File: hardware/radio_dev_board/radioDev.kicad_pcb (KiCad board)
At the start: 4 copper layers, 100 x 75 mm, 98 parts, among them J1 Conn_02x03_Odd_Even, J2 Conn_01x05, J3 Conn_01x05, J4 USB_C_Receptacle_USB2.0V1, J5 Barrel_Jack_MountingPin, J6 USB_C_Receptacle_USB2.0V1, Q1 Q_NPN_CBE, SW1 Reset, U1 SP3485CN, U10 LM1117-3.3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

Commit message: added program and misc buttons. Finish layout
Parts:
- added C32: 0.1, Capacitor_SMD:C_0603_1608Metric_Pad1.05x0.95mm_HandSolder, F.Cu at (159.1, 99.8)
- added G***: LOGO, libraries:4i_small_inv, F.Cu at (214.2, 118.0)
- added R27: 100K, Resistor_SMD:R_0603_1608Metric_Pad1.05x0.95mm_HandSolder, F.Cu at (204.8, 125.9)
- added R28: 100K, Resistor_SMD:R_0603_1608Metric_Pad1.05x0.95mm_HandSolder, F.Cu at (179.6, 125.9)
- added SW2: SW_Push, Button_Switch_SMD:SW_SPST_PTS645, F.Cu at (172.6, 129.1)
- added SW3: PGM, Button_Switch_SMD:SW_SPST_PTS645, F.Cu at (197.6, 129.1)
- added SW4: Misc, Button_Switch_SMD:SW_SPST_PTS645, F.Cu at (186.4, 129.1)
- D3: value OP1 -> 13
- D4: value OP2 -> A3
- D5: value OP3 -> A2
- D6: value OP4 -> A1
- D7: value OP5 -> A0
- moved R24 19.9 mm to (160.3, 127.0)
- moved D13 16.9 mm to (162.7, 131.2), turned to 270 degrees
- moved R23 16.7 mm to (162.7, 127.0)
- moved D14 16.7 mm to (160.3, 131.2), turned to 270 degrees
- moved R20 8.53 mm to (216.8, 83.3), turned to 180 degrees
- moved C2 7.19 mm to (152.4, 108.0), turned to 180 degrees
- moved R2 1.33 mm to (206.8, 86.5)
- moved C30 1.20 mm to (152.7, 121.7)
- moved R3 1.20 mm to (193.4, 85.0)
- moved C28 1.20 mm to (152.7, 125.1)
- moved C29 1.20 mm to (152.7, 123.4)
- moved C6 1.10 mm to (171.9, 103.6)
- moved C4 0.90 mm to (157.5, 104.2)
- moved U5 0.45 mm to (186.0, 101.5)
- moved C9 0.35 mm to (183.3, 106.0)
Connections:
- C5 pad 1: /~Reset -> /Arduino Controller/~Reset
- R8 pad 2: /~Reset -> /Arduino Controller/~Reset
- SW1 pad 1: /~Reset -> /Arduino Controller/~Reset
- U2 pad B14: (no net) -> /A4
- U4 pad 11: (no net) -> /A4
- U4 pad 12: (no net) -> Net-(R28-Pad2)
- U4 pad 13: (no net) -> Net-(R27-Pad2)
- U4 pad 29: /~Reset -> /Arduino Controller/~Reset
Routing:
- net /TXD: track 0.00 -> 71.6 mm, vias 0 -> 2
- net /RXD: track 0.00 -> 71.6 mm, vias 0 -> 2
- net /A4: track 0.00 -> 60.4 mm, vias 0 -> 2
- net Net-(R27-Pad2): track 0.00 -> 55.8 mm, vias 0 -> 2
- net /Arduino Controller/~Reset: track 0.00 -> 49.7 mm, vias 0 -> 2
- net /MOSI: track 12.1 -> 61.3 mm, vias 0 -> 1
- net /MISO: track 18.0 -> 64.0 mm, vias 0 -> 1
- net Net-(R28-Pad2): track 0.00 -> 45.6 mm, vias 0 -> 2
- net /SCK: track 30.8 -> 74.2 mm, vias 0 -> 1
- net GND: track 90.6 -> 120.8 mm, vias 55 -> 62
- net Net-(R23-Pad1): track 0.00 -> 20.4 mm
- net Net-(R24-Pad1): track 0.00 -> 18.6 mm
- net Net-(C27-Pad1): track 0.00 -> 12.2 mm
- net +5V: track 114.2 -> 121.8 mm, vias 16 -> 27
- net +3V3: track 66.2 -> 73.2 mm, vias 14 -> 15
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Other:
- board text added: "+5V"
- board text added: "13"
- board text added: "4i Systems"
- board text added: "A0"
- board text added: "A1"
- board text added: "A2"
- board text added: "A3"
- board text added: "DC 8-28V"
- board text added: "GND"
- board text added: "Local"
- board text added: "MISO"
- board text added: "MOSI"
- board text added: "Misc"
- board text added: "PGM"
- board text added: "RX"
- board text added: "Radio"
- board text added: "SCK"
- board text added: "TART 3 Development Board (c) Phill Brown 2019"
- board text added: "TX"
- board text added: "~Reset"
- board text added: "~Reset~-Local"
- board text added: "~Reset~-Radio"

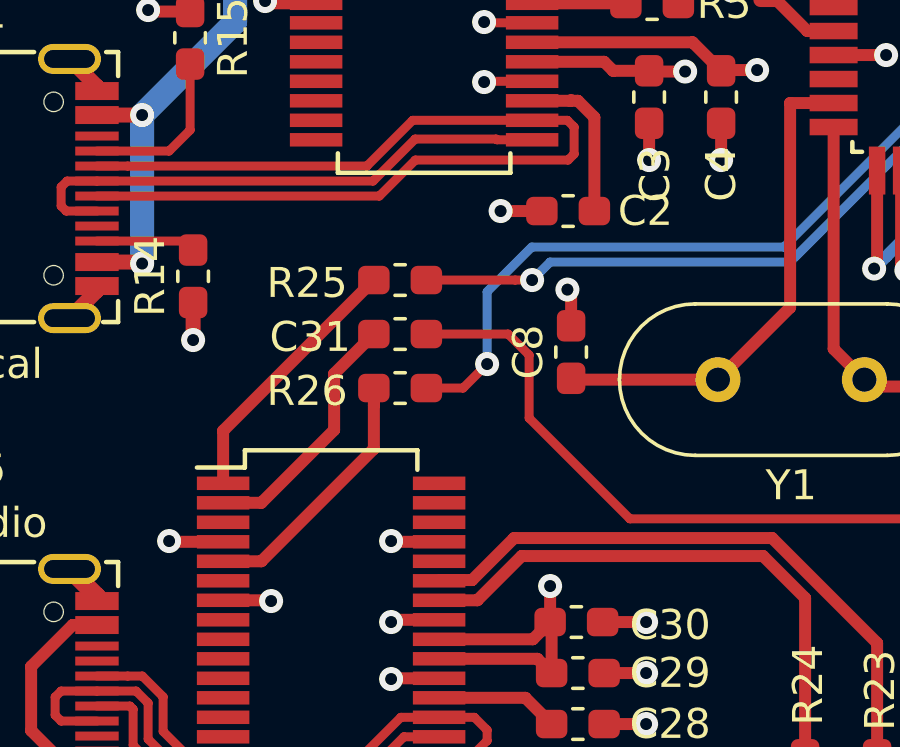
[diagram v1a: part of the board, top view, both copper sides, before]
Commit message: radio hub board started
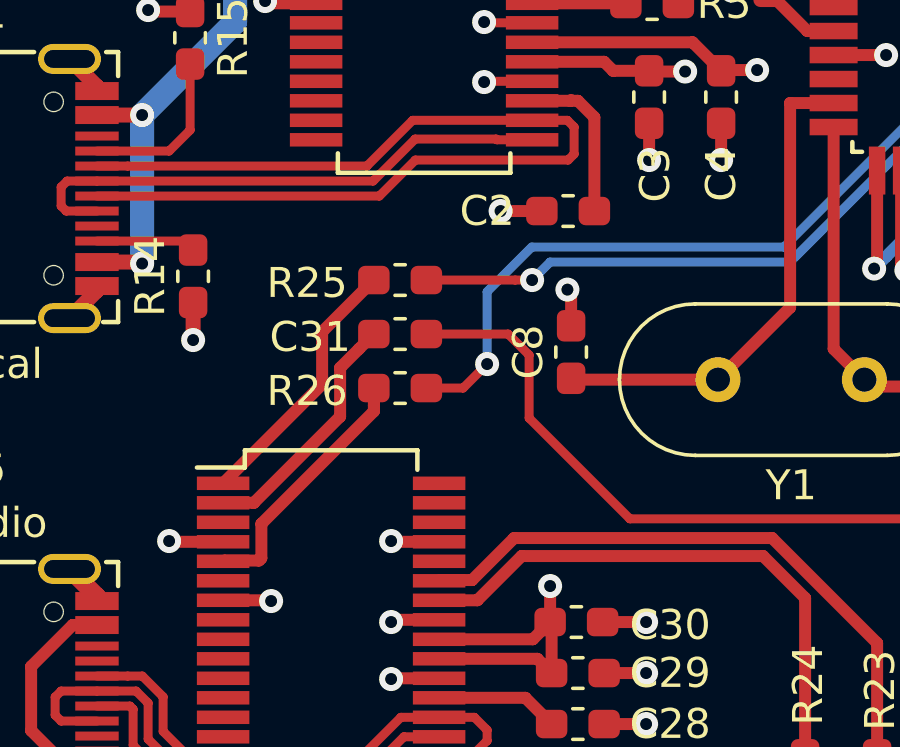
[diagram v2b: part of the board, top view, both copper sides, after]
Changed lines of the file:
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@@
-(kicad_pcb (version 20171130) (host pcbnew 5.1.4+dfsg1-2)
+(kicad_pcb (version 20171130) (host pcbnew 5.1.5+dfsg1-2)
   (general
     (thickness 1)
     (drawings 26)
-    (tracks 1005)
+    (tracks 1011)
     (zones 0)
     (modules 105)
@@
   )
   (setup
-    (last_trace_width 0.4)
+    (last_trace_width 0.25)
     (user_trace_width 0.2)
     (user_trace_width 0.3)
@@
       (outputformat 1)
       (mirror false)
-      (drillshape 1)
+      (drillshape 0)
       (scaleselection 1)
-      (outputdirectory ""))
+      (outputdirectory "eng/"))
   )
   (net 0 "")
@@
     (tags "capacitor handsolder")
     (attr smd)
-    (fp_text reference C2 (at -2.575 0) (layer F.SilkS)
+    (fp_text reference C2 (at 2.7 0) (layer F.SilkS)
       (effects (font (size 1 1) (thickness 0.15)))
     )
@@
   (segment (start 150.975 124.225) (end 151.85 125.1) (width 0.4) (layer F.Cu) (net 72))
   (segment (start 148.1 124.225) (end 150.975 124.225) (width 0.4) (layer F.Cu) (net 72))
-  (segment (start 142.175 117.725) (end 144.6 115.3) (width 0.4) (layer F.Cu) (net 73))
-  (segment (start 140.9 117.725) (end 142.175 117.725) (width 0.4) (layer F.Cu) (net 73))
-  (segment (start 144.6 113.425) (end 145.925 112.1) (width 0.4) (layer F.Cu) (net 73))
-  (segment (start 144.6 115.3) (end 144.6 113.425) (width 0.4) (layer F.Cu) (net 73))
+  (segment (start 141.926458 117.725) (end 144.800011 114.851447) (width 0.4) (layer F.Cu) (net 73))
+  (segment (start 144.800011 113.224989) (end 145.425928 112.599072) (width 0.4) (layer F.Cu) (net 73))
+  (segment (start 144.800011 114.851447) (end 144.800011 113.224989) (width 0.4) (layer F.Cu) (net 73))
+  (segment (start 145.425928 112.599072) (end 145.925 112.1) (width 0.4) (layer F.Cu) (net 73))
+  (segment (start 140.9 117.725) (end 141.926458 117.725) (width 0.4) (layer F.Cu) (net 73))
   (segment (start 192.3 119.6) (end 192.3 117.2) (width 0.4) (layer F.Cu) (net 74))
   (segment (start 186.597096 114.200011) (end 188.150011 114.200011) (width 0.4) (layer F.Cu) (net 75))
@@
   (segment (start 160.3 120.9) (end 160.3 126.125) (width 0.4) (layer F.Cu) (net 84))
   (segment (start 158.9 119.5) (end 160.3 120.9) (width 0.4) (layer F.Cu) (net 84))
-  (segment (start 140.9 115.325) (end 145.925 110.3) (width 0.4) (layer F.Cu) (net 85))
-  (segment (start 140.9 117.075) (end 140.9 115.325) (width 0.4) (layer F.Cu) (net 85))
+  (segment (start 144.2 113.775) (end 144.2 112.025) (width 0.4) (layer F.Cu) (net 85))
+  (segment (start 144.2 112.025) (end 145.925 110.3) (width 0.4) (layer F.Cu) (net 85))
+  (segment (start 140.9 117.075) (end 144.2 113.775) (width 0.4) (layer F.Cu) (net 85))
   (via (at 151.2 110.3) (size 0.8) (drill 0.4) (layers F.Cu B.Cu) (net 86))
   (segment (start 150.634315 110.3) (end 147.675 110.3) (width 0.3) (layer F.Cu) (net 86))
@@
   (segment (start 168.014795 95.480196) (end 168.014795 96.045881) (width 0.3) (layer F.Cu) (net 86))
   (segment (start 200 87) (end 196.114244 87) (width 0.3) (layer F.Cu) (net 86))
-  (segment (start 145.925 115.925) (end 145.925 114.475) (width 0.4) (layer F.Cu) (net 87))
+  (segment (start 145.925 114.675) (end 145.925 114.475) (width 0.4) (layer F.Cu) (net 87))
+  (segment (start 140.925 119.675) (end 140.949999 119.650001) (width 0.4) (layer F.Cu) (net 87))
   (segment (start 145.925 114.475) (end 145.925 113.9) (width 0.4) (layer F.Cu) (net 87))
-  (segment (start 142.175 119.675) (end 145.925 115.925) (width 0.4) (layer F.Cu) (net 87))
-  (segment (start 140.9 119.675) (end 142.175 119.675) (width 0.4) (layer F.Cu) (net 87))
+  (segment (start 140.9 119.675) (end 140.925 119.675) (width 0.4) (layer F.Cu) (net 87))
+  (segment (start 140.949999 119.650001) (end 142.095001 119.650001) (width 0.4) (layer F.Cu) (net 87))
+  (segment (start 142.095001 119.650001) (end 142.175001 119.570001) (width 0.4) (layer F.Cu) (net 87))
+  (segment (start 142.175001 119.570001) (end 142.175001 118.424999) (width 0.4) (layer F.Cu) (net 87))
+  (segment (start 142.175001 118.424999) (end 145.925 114.675) (width 0.4) (layer F.Cu) (net 87))
   (via (at 149.7 113.1) (size 0.8) (drill 0.4) (layers F.Cu B.Cu) (net 88))
   (segment (start 149.7 113.1) (end 148.9 113.9) (width 0.3) (layer F.Cu) (net 88))
